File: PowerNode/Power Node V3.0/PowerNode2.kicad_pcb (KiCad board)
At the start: 2 copper layers, 78.4 x 64.8 mm, 64 parts, among them IC1 CD4511B, IC4 ACS712xLCTR-30A, IC5 74HC595N, IC7 CD4511B

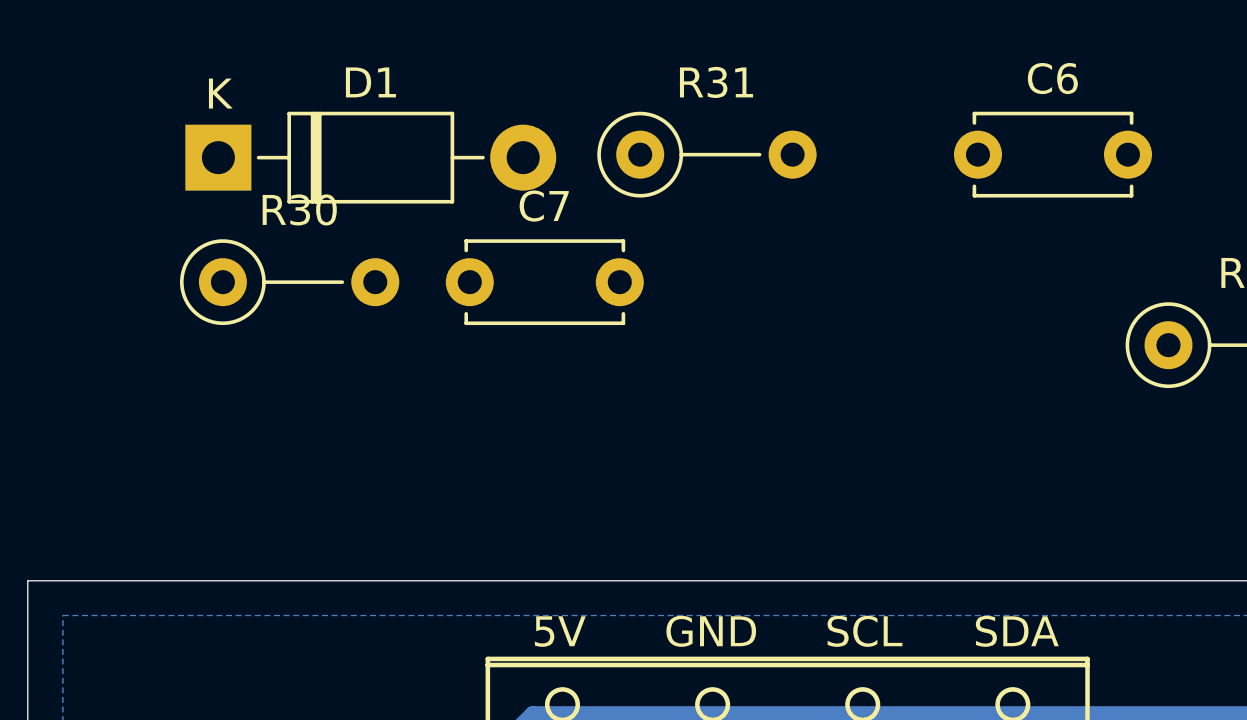
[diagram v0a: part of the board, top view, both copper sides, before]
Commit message: PN3: Fixes for SPICE simulation
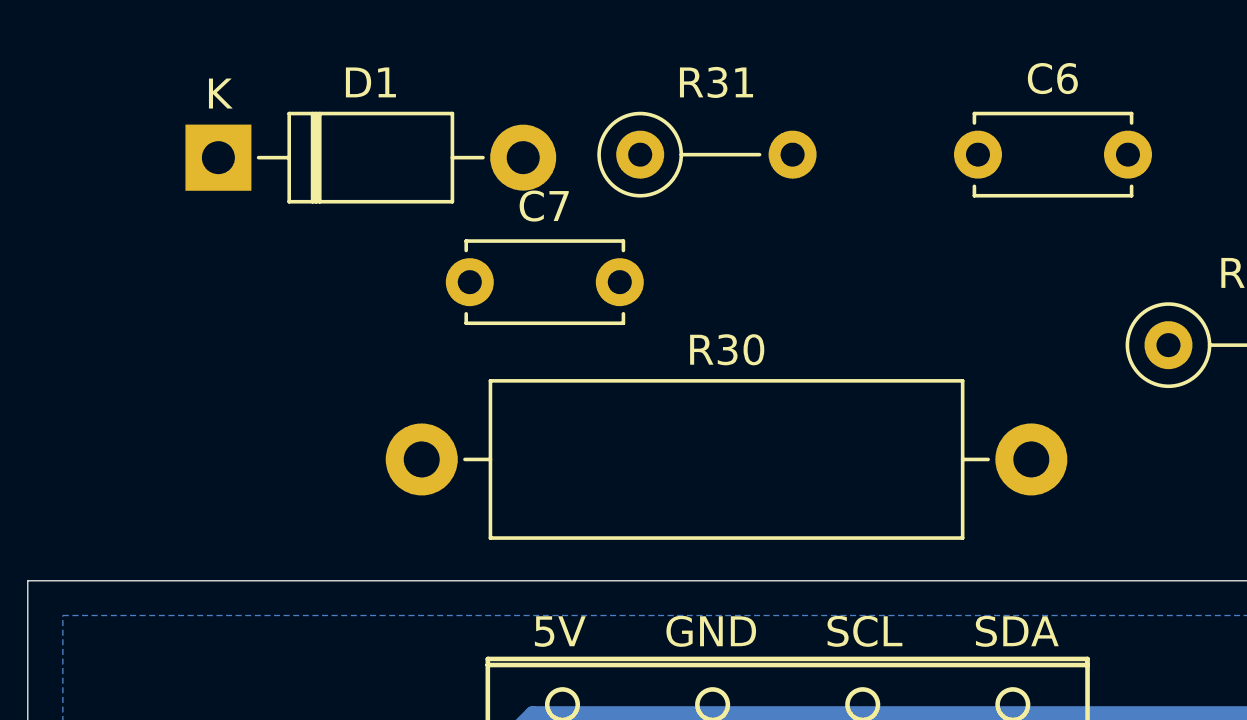
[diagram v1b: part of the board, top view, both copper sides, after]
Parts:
- D1: value 1N4733A -> 1N4732A
- R30: value 110 -> 220; footprint Resistor_THT:R_Axial_DIN0207_L6.3mm_D2.5mm_P5.08mm_Vertical -> Resistor_THT:R_Axial_DIN0516_L15.5mm_D5.0mm_P20.32mm_Horizontal
- moved R30 8.88 mm to (122.4, 68.6)
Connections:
- net /BL'1 renamed /nBL1
- net /BL'2 renamed /nBL2
- net /LE'1 renamed /nLE1
- net /LE'2 renamed /nLE2
- net /LT'1 renamed /nLT1
- net /LT'2 renamed /nLT2
- net /QH' renamed /nQH
- net Net-(D1-Pad1) renamed /Logic/VMEAS_IN

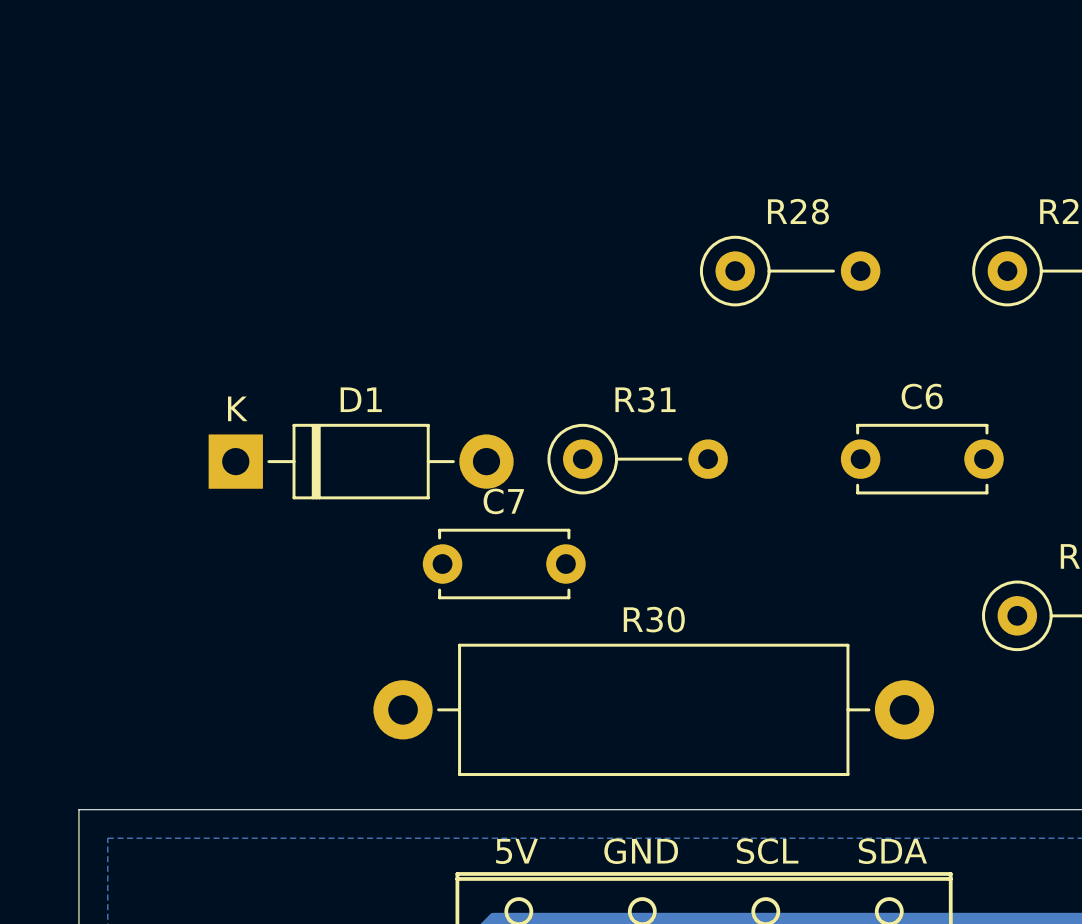
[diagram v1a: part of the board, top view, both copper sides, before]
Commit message: PN3: added voltage follower to VMEAS and removed zener diode
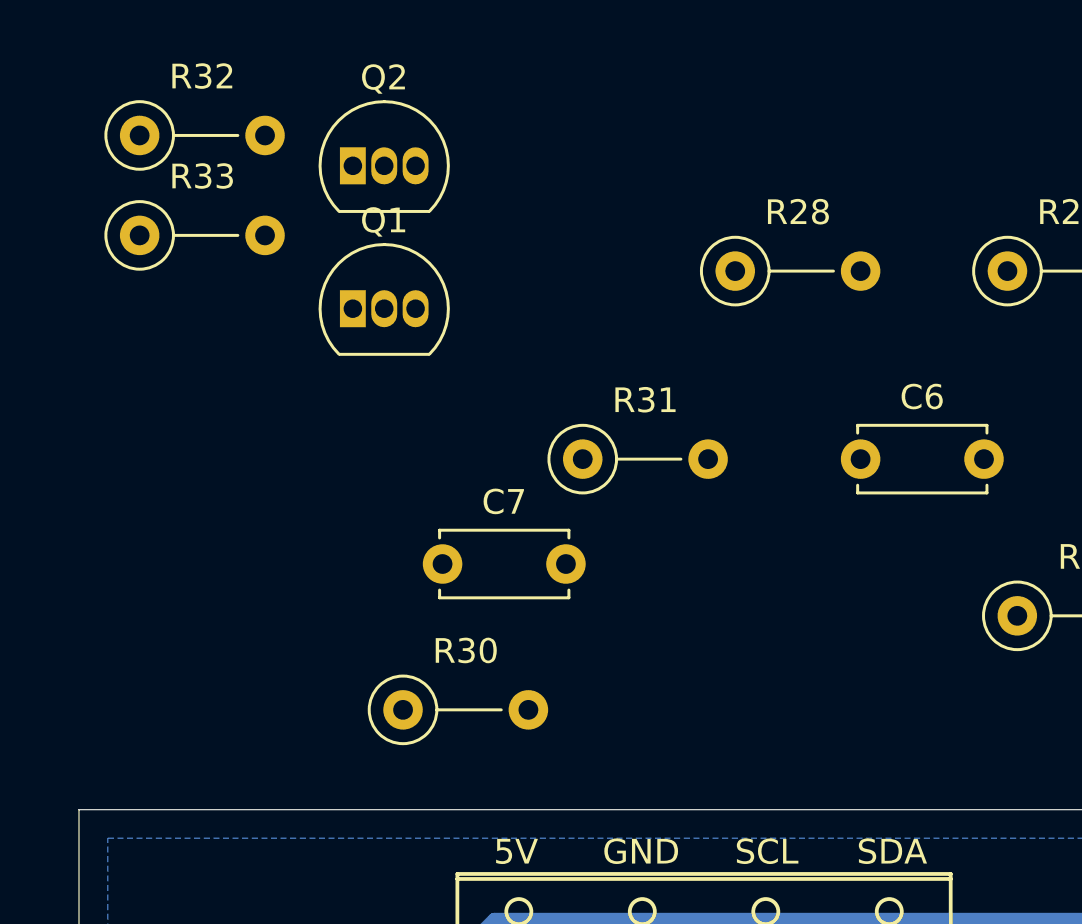
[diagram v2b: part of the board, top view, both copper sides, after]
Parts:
- removed D1: 1N4732A, Diode_THT:D_DO-41_SOD81_P10.16mm_Horizontal
- added Q1: 2N3904, Package_TO_SOT_THT:TO-92_Inline, F.Cu at (120.4, 52.3)
- added Q2: 2N3906, Package_TO_SOT_THT:TO-92_Inline, F.Cu at (120.4, 46.5)
- added R32: 10k, Resistor_THT:R_Axial_DIN0207_L6.3mm_D2.5mm_P5.08mm_Vertical, F.Cu at (111.8, 45.3)
- added R33: 10k, Resistor_THT:R_Axial_DIN0207_L6.3mm_D2.5mm_P5.08mm_Vertical, F.Cu at (111.8, 49.4)
- R30: value 220 -> 10k; footprint Resistor_THT:R_Axial_DIN0516_L15.5mm_D5.0mm_P20.32mm_Horizontal -> Resistor_THT:R_Axial_DIN0207_L6.3mm_D2.5mm_P5.08mm_Vertical
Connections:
- R30 pad 1: /Logic/VMEAS_IN -> /VMEAS
- R30 pad 2: /VMEAS -> Net-(Q1-Pad2)
- U$1 pad 6: /Logic/VMEAS_IN -> /VMEAS_1

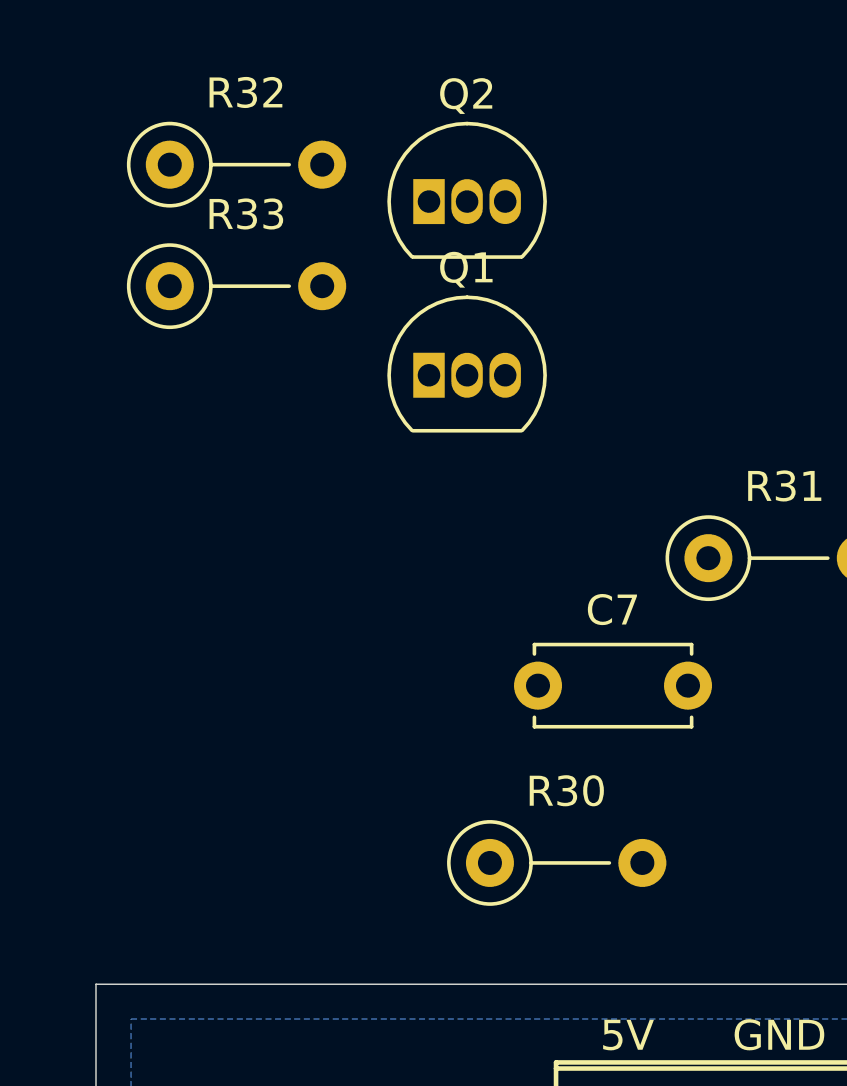
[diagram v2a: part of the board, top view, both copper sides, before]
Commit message: Removed BJTs and connected VMEAS directly
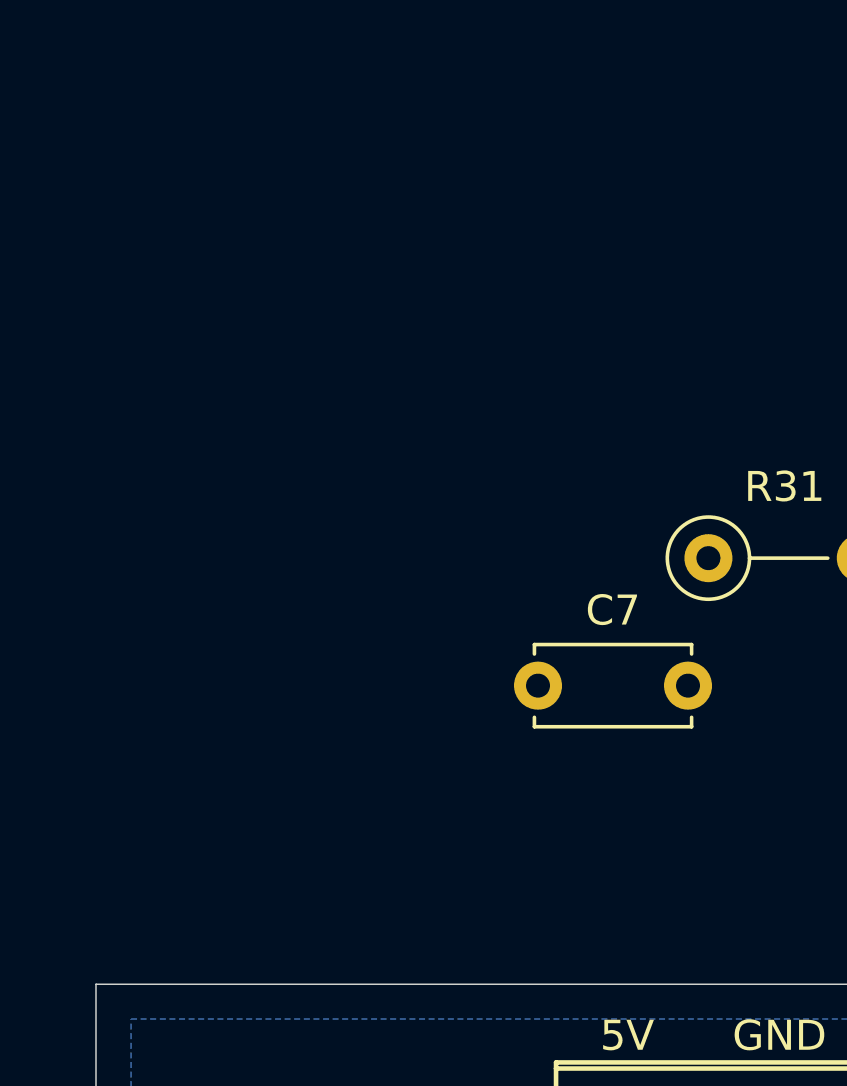
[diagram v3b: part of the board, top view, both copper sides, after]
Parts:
- removed Q1: 2N3904, Package_TO_SOT_THT:TO-92_Inline
- removed Q2: 2N3906, Package_TO_SOT_THT:TO-92_Inline
- removed R30, R32, R33: 10k, Resistor_THT:R_Axial_DIN0207_L6.3mm_D2.5mm_P5.08mm_Vertical
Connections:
- U$1 pad 6: /VMEAS_1 -> /VMEAS

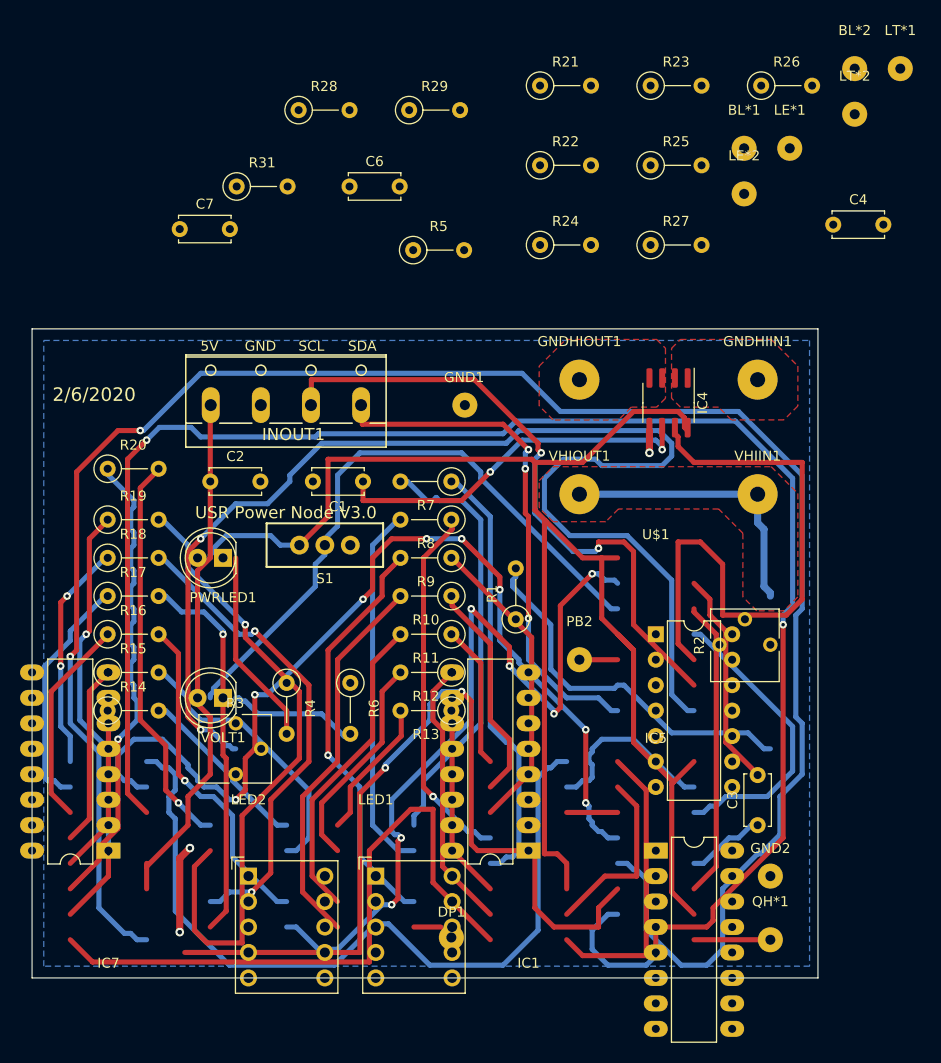
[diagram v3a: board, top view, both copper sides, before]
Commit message: PN3: changed resistors to use SMD footprints
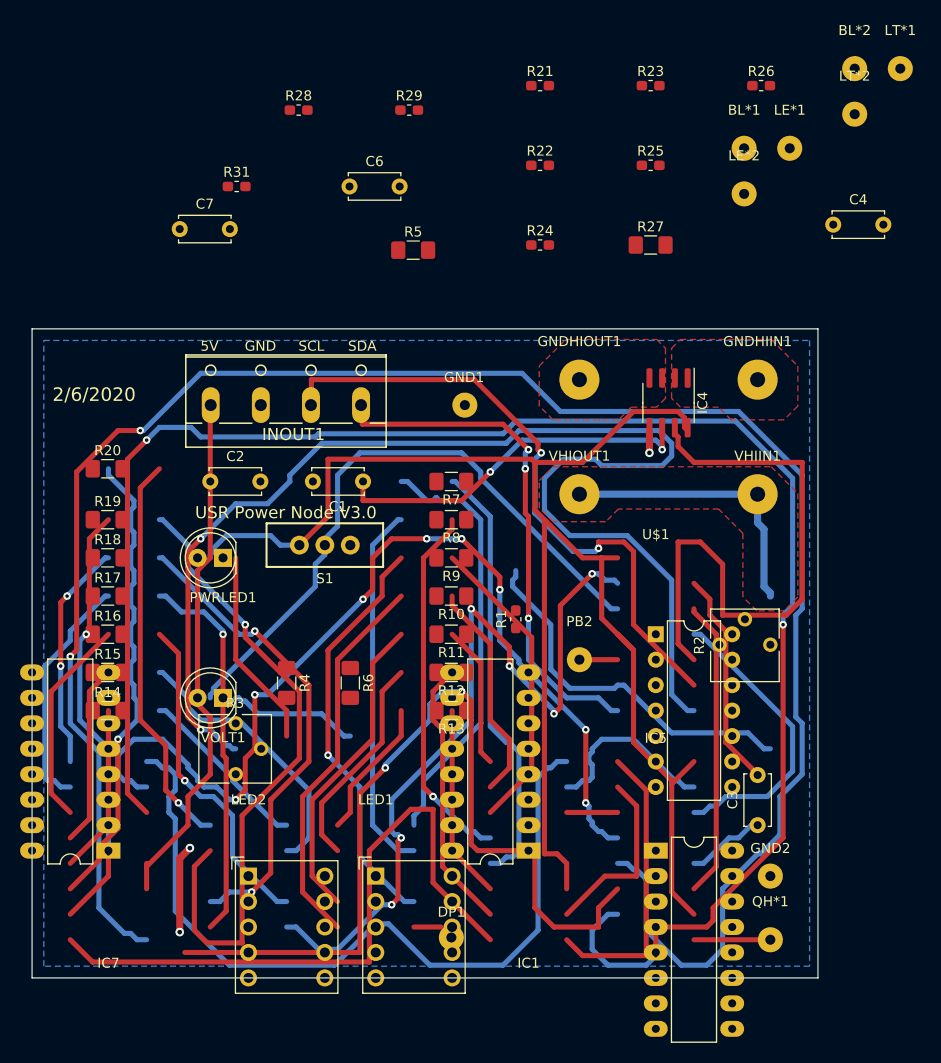
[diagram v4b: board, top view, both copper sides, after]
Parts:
- R1, R21, R22, R23, R24, R25, R26, R28, R29, R31: footprint Resistor_THT:R_Axial_DIN0207_L6.3mm_D2.5mm_P5.08mm_Vertical -> Resistor_SMD:R_0603_1608Metric_Pad1.05x0.95mm_HandSolder
- R10, R11, R12, R13, R14, R15, R16, R17, R18, R19, R20, R27, R4, R5, R6, R7, R8, R9: footprint Resistor_THT:R_Axial_DIN0207_L6.3mm_D2.5mm_P5.08mm_Vertical -> Resistor_SMD:R_1206_3216Metric_Pad1.42x1.75mm_HandSolder
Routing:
- net Vdd: track 0.00 -> 54.6 mm
- net Net-(R6-Pad2): track 13.0 -> 51.1 mm, vias 0 -> 1
- net Net-(LED2-Pad5): track 38.1 -> 0.00 mm
- net /VMEAS: track 37.0 -> 0.00 mm
- net Vss: track 2.16 -> 30.0 mm
- net Net-(LED2-Pad9): track 27.9 -> 0.00 mm
- net Net-(LED2-Pad10): track 17.6 -> 0.00 mm
- net /d2: vias 1 -> 0

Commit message: PN3: removed R2 and replaced with a switched voltage divider
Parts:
- added 5V1: LED5MM, LED_THT:LED_D5.0mm, F.Cu at (122.9, 49.8)
- added R30: 220, Resistor_SMD:R_1206_3216Metric_Pad1.42x1.75mm_HandSolder, F.Cu at (123.4, 55.2)
- added R32: 10k, Resistor_SMD:R_0603_1608Metric_Pad1.05x0.95mm_HandSolder, F.Cu at (111.2, 56.1)
- added R33: 10k, Resistor_SMD:R_0603_1608Metric_Pad1.05x0.95mm_HandSolder, F.Cu at (115.5, 56.1)
- added S2: SW_DPDT_x2, OSx02011MS2Qx1:OS202011MS2Qx1, F.Cu at (114.7, 50.8)
- R2: value TRIM_US-B25P -> 43k; footprint Potentiometer_THT:Potentiometer_Vishay_T73YP_Vertical -> Resistor_SMD:R_0603_1608Metric_Pad1.05x0.95mm_HandSolder
- S1: footprint PowerNode2:SWITCH_SPDT_PTH_11.6X4.0MM -> OSx02011MS2Qx1:OS102011MS2Qx1
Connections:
- C4 pad 1: /VMEAS -> /VMEAS_1
- R2 pad 1: /VHI -> Net-(R2-Pad1)
- R2 pad 2: /VMEAS -> /VHI
- U$1 pad 6: /VMEAS -> /VMEAS_1
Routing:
- net Net-(IC4-Pad7): track 0.00 -> 59.8 mm
- net /IMEAS: track 59.8 -> 0.00 mm

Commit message: PN3: reannotated schematic and updated board
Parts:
- S1: renamed from S2; value SW_DPDT_x2 -> SW_DPDT
- renumbered C4 to C2, C6 to C3, C3 to C4, C7 to C5, C2 to C6, IC4 to IC1, IC5 to IC2, IC1 to IC3, IC7 to IC4, PB2 to PB1, R2 to R1, R5 to R10, R31 to R11, R28 to R12, R25 to R13, R21 to R14, R22 to R15, R26 to R16, R23 to R17, R24 to R18, R7 to R19, R30 to R2, R8 to R20, R9 to R21, R10 to R22, R11 to R23, R12 to R24, R13 to R25, R29 to R26, R14 to R27, R15 to R28, R16 to R29, R32 to R3, R17 to R30, R18 to R31, R19 to R32, R20 to R33, R33 to R5, R1 to R6, R3 to R7, R6 to R8, R27 to R9, S1 to S2
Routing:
- net Net-(IC5-Pad5): track 0.00 -> 201.3 mm
- net Net-(IC2-Pad5): track 201.3 -> 0.00 mm
- net Net-(IC5-Pad7): track 0.00 -> 175.9 mm
- net Net-(IC2-Pad7): track 175.9 -> 0.00 mm
- net Net-(IC5-Pad4): track 0.00 -> 97.8 mm
- net Net-(IC2-Pad4): track 97.8 -> 0.00 mm
- net Net-(IC5-Pad6): track 0.00 -> 88.5 mm
- net Net-(IC2-Pad6): track 88.5 -> 0.00 mm
- net Net-(IC7-Pad14): track 0.00 -> 47.2 mm
- net Net-(IC4-Pad14): track 47.2 -> 0.00 mm
- net Net-(IC3-Pad13): track 43.3 -> 0.00 mm
- net Net-(IC1-Pad13): track 0.00 -> 43.3 mm
- net Net-(IC7-Pad15): track 0.00 -> 43.3 mm
- net Net-(IC4-Pad15): track 43.3 -> 0.00 mm
- net Net-(IC3-Pad12): track 36.6 -> 0.00 mm
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
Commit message: PN3: connected 5V indicator to PB2 and other small changes
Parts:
- removed PB1: 2,54_0,9, Connector_Wire:SolderWirePad_1x01_Drill1mm
- removed PWRLED1: LED5MM, LED_THT:LED_D5.0mm
- added PWR1: LED5MM, LED_THT:LED_D5.0mm, F.Cu at (114.3, 64.5)
- R7: value TRIM_US-B25P -> 100k
- renumbered 5V1 to VDIV1
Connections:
- S1 pad 1: Vdd -> Vss
- S1 pad 2: Net-(5V1-Pad2) -> /VDIV
- S1 pad 3: Vss -> Vdd
- U$1 pad 5: /PB2 -> /VDIV
- VDIV1 pad 2: Net-(5V1-Pad2) -> /VDIV
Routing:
- net Net-(PWRLED1-Pad1): track 0.00 -> 19.9 mm
- net Net-(PWR1-Pad1): track 19.9 -> 0.00 mm
- added copper zone on F.Cu, net Net-(R2-Pad2)
- removed copper zone on F.Cu, net Net-(R2-Pad2) (its old number)
